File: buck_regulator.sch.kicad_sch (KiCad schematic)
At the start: 4 parts, among them U1 XL1509-12

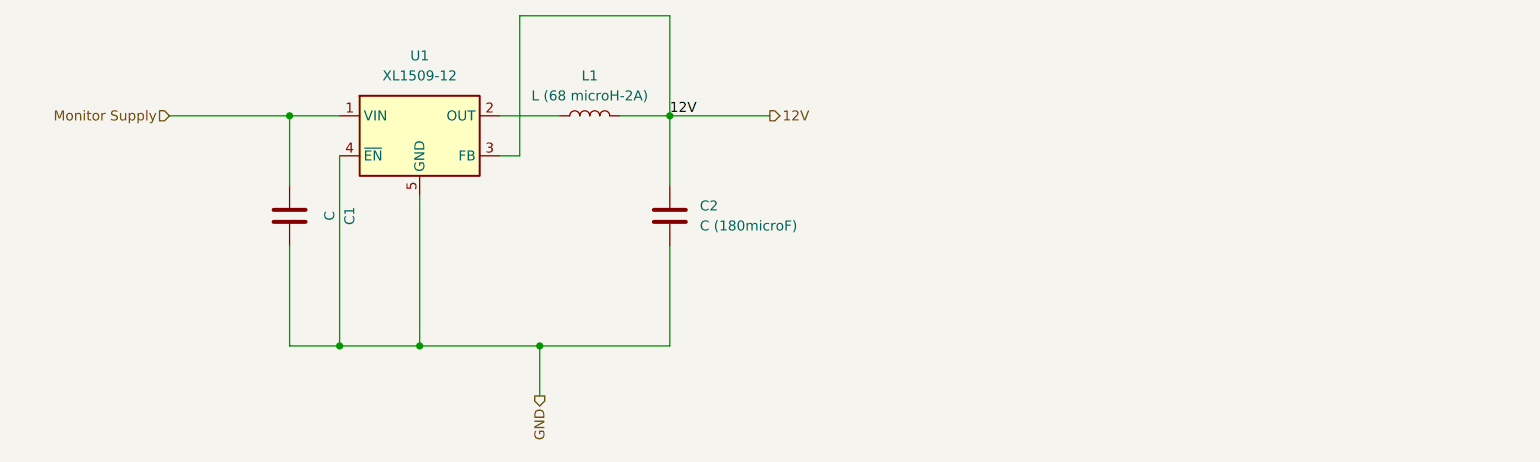
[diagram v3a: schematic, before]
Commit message: Schematic Complete
Completed the wiring of the circuit.

(Missing some labels and footprints)
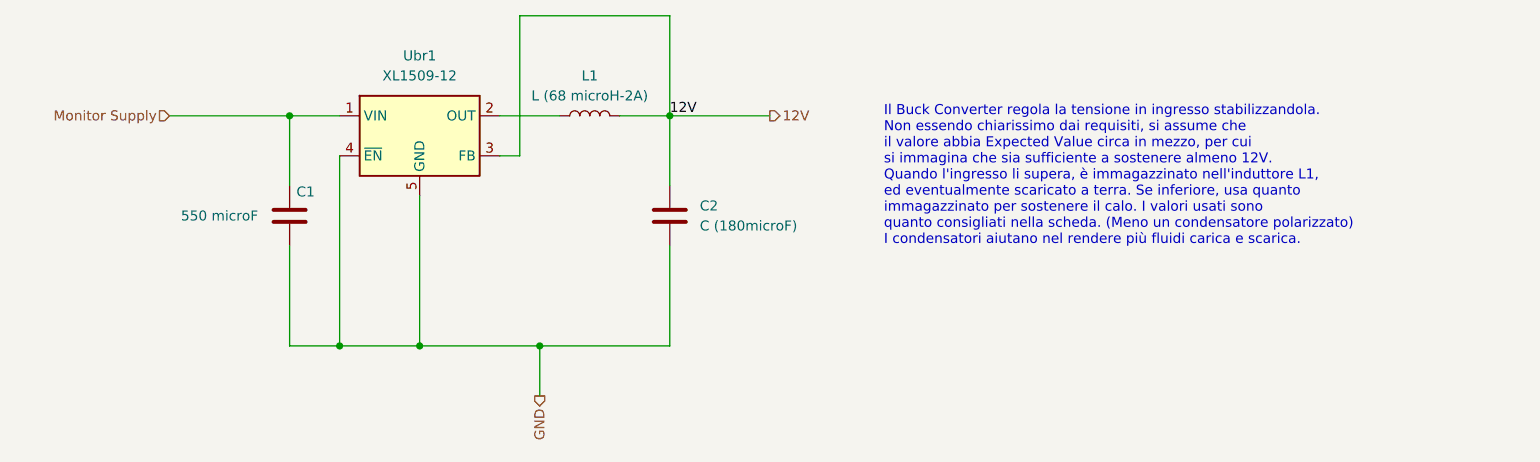
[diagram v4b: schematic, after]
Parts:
- C1: value C -> 550 microF; footprint (none) -> Capacitor_SMD:C_0201_0603Metric_Pad0.64x0.40mm_HandSolder
- C2: footprint (none) -> Capacitor_SMD:C_0603_1608Metric_Pad1.08x0.95mm_HandSolder
- renumbered U1 to Ubr1
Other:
- note added: "Il Buck Converter regola la tensione in ingresso stabilizzandola. Non essendo chiarissimo dai requisiti, si assume che il valore abbia Expected Value circa in mezzo, per cui si immagina che sia sufficiente a sostenere almeno 12V. Quando l'ingresso li supera, è immagazzinato nell'induttore L1, ed eventualmente scaricato a terra. Se inferiore, usa quanto immagazzinato per sostenere il calo. I valor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"
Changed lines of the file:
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@@
 	(generator_version "9.0")
 	(paper "A4")
+	(text "Il Buck Converter regola la tensione in ingresso stabilizzandola.\nNon essendo chiarissimo dai requisiti, si assume che\nil valore abbia Expected Value circa in mezzo, per cui\nsi immagina che sia sufficiente a sostenere almeno 12V. \nQuando l'ingresso li supera, è immagazzinato nell'induttore L1,\ned eventualmente scaricato a terra. Se inferiore, usa quanto\nimmagazzinato per sostenere il calo. I valori usati sono\nquanto consigliati nella scheda. (Meno un condensatore polarizzato)\nI condensatori aiutano nel rendere più fluidi carica e scarica."
+		(exclude_from_sim no)
+		(at 187.198 86.36 0)
+		(effects
+			(font
+				(size 1.27 1.27)
+			)
+			(justify left)
+		)
+	)
 	(junction
 		(at 143.51 107.95)
@@
 			)
 		)
-		(property "Footprint" ""
+		(property "Footprint" "Capacitor_SMD:C_0603_1608Metric_Pad1.08x0.95mm_HandSolder"
 			(at 160.9852 95.25 0)
 			(effects
@@
 		(on_board yes)
 		(dnp no)
-		(fields_autoplaced yes)
 		(property "Reference" "C1"
-			(at 119.38 91.44 90)
-			(effects
-				(font
-					(size 1.27 1.27)
-				)
-			)
-		)
-		(property "Value" "C"
-			(at 116.84 91.44 90)
-			(effects
-				(font
-					(size 1.27 1.27)
-				)
-			)
-		)
-		(property "Footprint" ""
+			(at 113.792 88.392 0)
+			(effects
+				(font
+					(size 1.27 1.27)
+				)
+			)
+		)
+		(property "Value" "550 microF"
+			(at 102.87 91.44 0)
+			(effects
+				(font
+					(size 1.27 1.27)
+				)
+			)
+		)
+		(property "Footprint" "Capacitor_SMD:C_0201_0603Metric_Pad0.64x0.40mm_HandSolder"
 			(at 112.7252 95.25 0)
 			(effects
@@
 		(dnp no)
 		(fields_autoplaced yes)
-		(property "Reference" "U1"
+		(property "Reference" "Ubr1"
 			(at 128.27 71.12 0)
 			(effects
@@
 			(project "recruitment"
 				(path "/bdc7face-9f7c-4701-80bb-4cc144448db1/bc78e43e-7c72-4a26-8058-1235020e2308"
-					(reference "U1")
+					(reference "Ubr1")
 					(unit 1)
 				)

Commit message: Finished (?)
Assigned al values, footprints and generated traces.
Generated DRL files.
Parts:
- L1: footprint (none) -> Inductor_SMD:L_12x12mm_H8mm
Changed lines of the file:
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@@
 			)
 		)
-		(property "Footprint" ""
+		(property "Footprint" "Inductor_SMD:L_12x12mm_H8mm"
 			(at 149.86 78.74 0)
 			(effects
